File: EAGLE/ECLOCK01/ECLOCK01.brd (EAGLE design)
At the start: 100 x 54 mm, 12 parts

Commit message: FInal version of clock PCB before sending to board house
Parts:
- removed JP1: POWER_JACKCOMBO, SparkFun-Connectors:POWER_JACK_COMBO
- removed L1, L2, L3, L4: WS2812B, adafruit:WS2812B
- added C10, C11, C12, C13, C14, C15, C16, C17, C18, C19, C20, C21, C22, C23, C24, C25, C26, C27, C28, C29, C30, C31, C32, C33, C34, C35, C36, C37, C38, C39, C41, C42, C43, C44, C45, C46, C47, C48, C49, C50, C51, C52, C53, C54, C6, C7, C8, C9: 0.1, TinWhiskers:0805
- added C400, C401: 470, adafruit:PANASONIC_E
- added FID1, FID2: FIDUCIAL, TinWhiskers:FIDUCIAL
- added JP2: USB-MICROB, SparkFun-Connectors:USB-MICROB
- added LED1, LED10, LED11, LED12, LED13, LED14, LED15, LED16, LED17, LED18, LED19, LED2, LED20, LED21, LED22, LED23, LED24, LED25, LED26, LED27, LED28, LED29, LED3, LED30, LED31, LED32, LED33, LED34, LED35, LED36, LED37, LED38, LED39, LED4, LED40, LED41, LED42, LED43, LED44, LED45, LED46, LED47, LED48, LED49, LED5, LED50, LED51, LED52, LED53, LED54, LED6, LED7, LED8, LED9: WS2812B, GinWhiskers - temp stuff:WS2812B
- C1, C2, C3: value CAPACITOR0805 -> 0.1
- C4, C5: value 470 -> 0.1; device adafruit:PANASONIC_E -> TinWhiskers:0805
- U$1: device adafruit:ARDUINO -> GinWhiskers - temp stuff:ARDUINO-UNO
- moved C4 86.1 mm to (5.00, 32.0)
- moved C5 62.9 mm to (8.50, 32.0), turned to 180 degrees
- moved C1 33.5 mm to (7.00, 48.0), turned to 180 degrees
- moved C2 20.2 mm to (15.0, 48.0), turned to 180 degrees
- moved R1 20.1 mm to (28.5, 50.0), turned to 180 degrees
- moved C3 19.0 mm to (23.0, 48.0), turned to 180 degrees
- moved U$1 9.06 mm to (28.0, 1.00)
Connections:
- removed net N$6: L3.2-DOUT, L4.4-DIN
- new net N$10: LED15.2-DOUT, LED16.4-DIN
- new net N$12: LED18.4-DIN, LED53.2-DOUT
- new net N$13: LED19.2-DOUT, LED20.4-DIN
- new net N$14: LED17.4-DIN, LED18.2-DOUT
- new net N$15: LED19.4-DIN, LED8.2-DOUT
- new net N$16: LED47.2-DOUT, LED49.4-DIN
- new net N$17: LED39.2-DOUT, LED50.4-DIN
- new net N$18: LED24.2-DOUT, LED25.4-DIN
- new net N$19: LED25.2-DOUT, LED26.4-DIN
- new net N$2: LED11.2-DOUT, LED12.4-DIN
- new net N$20: LED13.2-DOUT, LED24.4-DIN
- new net N$21: LED27.2-DOUT, LED28.4-DIN
- new net N$22: LED28.2-DOUT, LED29.4-DIN
- new net N$25: LED40.2-DOUT, LED41.4-DIN
- new net N$26: LED20.2-DOUT, LED21.4-DIN
- new net N$27: LED11.4-DIN, LED9.2-DOUT
- new net N$28: LED17.2-DOUT, LED5.4-DIN
- new net N$29: LED4.4-DIN, LED5.2-DOUT
- new net N$30: LED6.2-DOUT, LED7.4-DIN
- new net N$31: LED7.2-DOUT, LED8.4-DIN
- new net N$32: LED21.2-DOUT, LED32.4-DIN
- new net N$33: LED48.4-DIN, LED49.2-DOUT
- new net N$34: LED36.4-DIN, LED48.2-DOUT
- new net N$36: LED37.2-DOUT, LED38.4-DIN
- new net N$37: LED38.2-DOUT, LED39.4-DIN
- new net N$39: LED30.2-DOUT, LED53.4-DIN
- new net N$40: LED34.2-DOUT, LED45.4-DIN
- new net N$41: LED32.2-DOUT, LED33.4-DIN
- new net N$42: LED33.2-DOUT, LED34.4-DIN
- new net N$44: LED31.4-DIN, LED43.2-DOUT
- new net N$45: LED4.2-DOUT, LED6.4-DIN
- new net N$46: LED46.2-DOUT, LED47.4-DIN
- new net N$47: LED45.2-DOUT, LED46.4-DIN
- new net N$48: LED42.2-DOUT, LED44.4-DIN
- new net N$49: LED43.4-DIN, LED44.2-DOUT
- new net N$50: LED30.4-DIN, LED31.2-DOUT
- new net N$51: LED41.2-DOUT, LED42.4-DIN
- new net N$52: LED35.4-DIN, LED36.2-DOUT
- new net N$53: LED35.2-DOUT, LED54.4-DIN
- new net N$54: LED50.2-DOUT, LED51.4-DIN
- new net N$55: LED51.2-DOUT, LED52.4-DIN
- new net N$56: LED23.4-DIN, LED54.2-DOUT
- new net N$58: LED22.4-DIN, LED23.2-DOUT
- new net N$59: LED14.4-DIN, LED3.2-DOUT
- new net N$60: LED10.4-DIN, LED22.2-DOUT
- new net N$61: LED10.2-DOUT, LED9.4-DIN
- new net N$62: LED29.2-DOUT, LED40.4-DIN
- new net N$7: LED12.2-DOUT, LED13.4-DIN
- new net N$8: LED26.2-DOUT, LED37.4-DIN
- new net N$9: LED14.2-DOUT, LED15.4-DIN
- new net VDD: C1.1, C10.1, C11.1, C12.1, C13.1, C14.1, C15.1, C16.1, C17.1, C18.1, C19.1, C2.1, C20.1, C21.1, C22.1, C23.1, C24.1, C25.1, C26.1, C27.1, C28.1, C29.1, C3.1, C30.1, C31.1, C32.1, C33.1, C34.1, C35.1, C36.1, C37.1, C38.1, C39.1, C4.1, C400.+, C401.+, C41.1, C42.1, C43.1, C44.1, C45.1, C46.1, C47.1, C48.1, C49.1, C5.1, C50.1, C51.1, C52.1, C53.1, C54.1, C6.1, C7.1, C8.1, C9.1, JP2.VBUS, LED1.1-VDD, LED10.1-VDD, LED11.1-VDD, LED12.1-VDD, LED13.1-VDD, LED14.1-VDD, LED15.1-VDD, LED16.1-VDD, LED17.1-VDD, LED18.1-VDD, LED19.1-VDD, LED2.1-VDD, LED20.1-VDD, LED21.1-VDD, LED22.1-VDD, LED23.1-VDD, LED24.1-VDD, LED25.1-VDD, LED26.1-VDD, LED27.1-VDD, LED28.1-VDD, LED29.1-VDD, LED3.1-VDD, LED30.1-VDD, LED31.1-VDD, LED32.1-VDD, LED33.1-VDD, LED34.1-VDD, LED35.1-VDD, LED36.1-VDD, LED37.1-VDD, LED38.1-VDD, LED39.1-VDD, LED4.1-VDD, LED40.1-VDD, LED41.1-VDD, LED42.1-VDD, LED43.1-VDD, LED44.1-VDD, LED45.1-VDD, LED46.1-VDD, LED47.1-VDD, LED48.1-VDD, LED49.1-VDD, LED5.1-VDD, LED50.1-VDD, LED51.1-VDD, LED52.1-VDD, LED53.1-VDD, LED54.1-VDD, LED6.1-VDD, LED7.1-VDD, LED8.1-VDD, LED9.1-VDD
- net GND: now also C1.2, C10.2, C11.2, C12.2, C13.2, C14.2, C15.2, C16.2, C17.2, C18.2, C19.2, C2.2, C20.2, C21.2, C22.2, C23.2, C24.2, C25.2, C26.2, C27.2, C28.2, C29.2, C3.2, C30.2, C31.2, C32.2, C33.2, C34.2, C35.2, C36.2, C37.2, C38.2, C39.2, C4.2, C400.-, C401.-, C41.2, C42.2, C43.2, C44.2, C45.2, C46.2, C47.2, C48.2, C49.2, C5.2, C50.2, C51.2, C52.2, C53.2, C54.2, C6.2, C7.2, C8.2, C9.2, JP2.GND, JP2.MT1, JP2.MT2, LED1.3-GND, LED10.3-GND, LED11.3-GND, LED12.3-GND, LED13.3-GND, LED14.3-GND, LED15.3-GND, LED16.3-GND, LED17.3-GND, LED18.3-GND, LED19.3-GND, LED2.3-GND, LED20.3-GND, LED21.3-GND, LED22.3-GND, LED23.3-GND, LED24.3-GND, LED25.3-GND, LED26.3-GND, LED27.3-GND, LED28.3-GND, LED29.3-GND, LED3.3-GND, LED30.3-GND, LED31.3-GND, LED32.3-GND, LED33.3-GND, LED34.3-GND, LED35.3-GND, LED36.3-GND, LED37.3-GND, LED38.3-GND, LED39.3-GND, LED4.3-GND, LED40.3-GND, LED41.3-GND, LED42.3-GND, LED43.3-GND, LED44.3-GND, LED45.3-GND, LED46.3-GND, LED47.3-GND, LED48.3-GND, LED49.3-GND, LED5.3-GND, LED50.3-GND, LED51.3-GND, LED52.3-GND, LED53.3-GND, LED54.3-GND, LED6.3-GND, LED7.3-GND, LED8.3-GND, LED9.3-GND; no longer C4.-, C5.-, JP1.GND, JP1.GND@1, L1.3-GND, L2.3-GND, L3.3-GND, L4.3-GND
- net LED_IN: now also U$1.D13; no longer U$1.D0
- net N$1: now also LED1.4-DIN; no longer L1.4-DIN
- net N$3: now also LED1.2-DOUT, LED2.4-DIN; no longer L1.2-DOUT, L2.4-DIN
- net N$4: now also LED2.2-DOUT, LED3.4-DIN; no longer L2.2-DOUT, L3.4-DIN
- net N$5: now also LED16.2-DOUT, LED27.4-DIN; no longer C4.+, C5.+, JP1.POWER, L1.1-VDD, L2.1-VDD, L3.1-VDD, L4.1-VDD
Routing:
- net GND: track 0.00 -> 271.3 mm, vias 0 -> 62
- net N$1: track 0.00 -> 29.6 mm
- net LED_IN: track 0.00 -> 28.8 mm, vias 0 -> 1
- net N$8: track 0.00 -> 24.5 mm
- net N$5: track 0.00 -> 24.5 mm
- net N$32: track 0.00 -> 24.5 mm
- net N$61: track 0.00 -> 12.5 mm
- net N$29: track 0.00 -> 12.5 mm
- net N$58: track 0.00 -> 12.5 mm
- net N$14: track 0.00 -> 12.5 mm
- net N$52: track 0.00 -> 12.5 mm
- net N$50: track 0.00 -> 12.5 mm
- net N$49: track 0.00 -> 12.5 mm
- net N$33: track 0.00 -> 12.5 mm
- net N$45: track 0.00 -> 11.7 mm, vias 0 -> 2
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- added copper zone on layer 1, net GND
- added copper zone on layer 16, net GND
- added copper zone on layer 1, net VDD
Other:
- board size 100 x 54 mm -> 135 x 55 mm

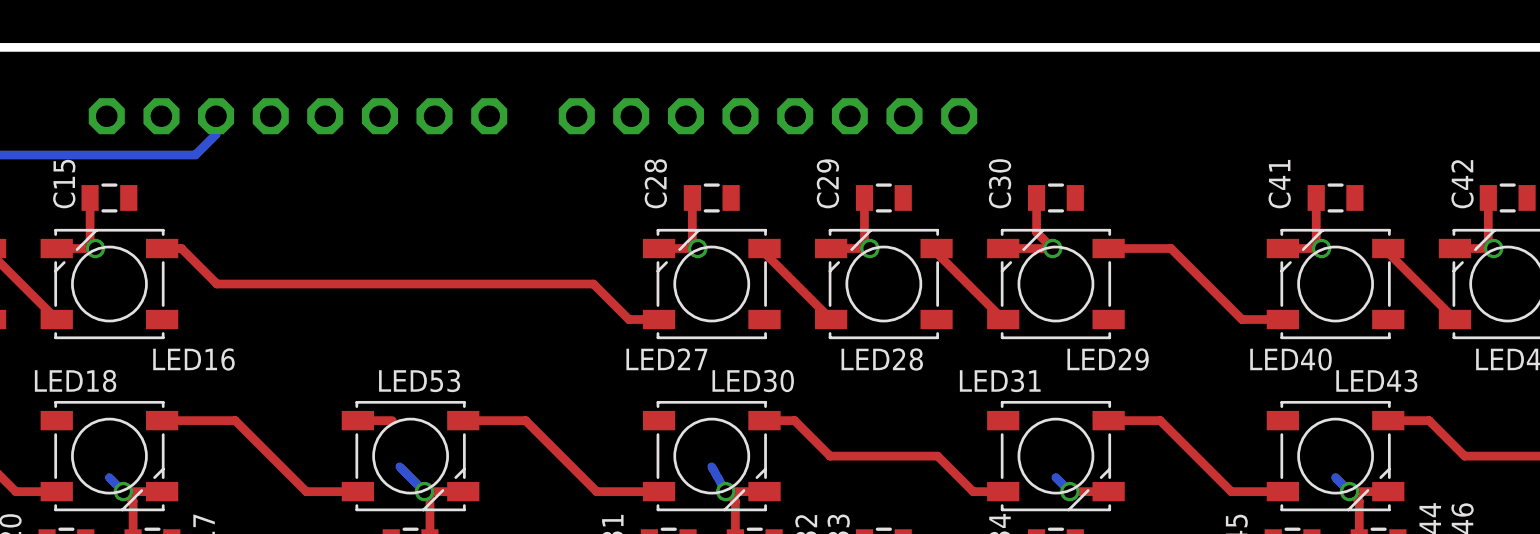
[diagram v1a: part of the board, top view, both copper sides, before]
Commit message: Added two pushbuttons and a connector for the horn
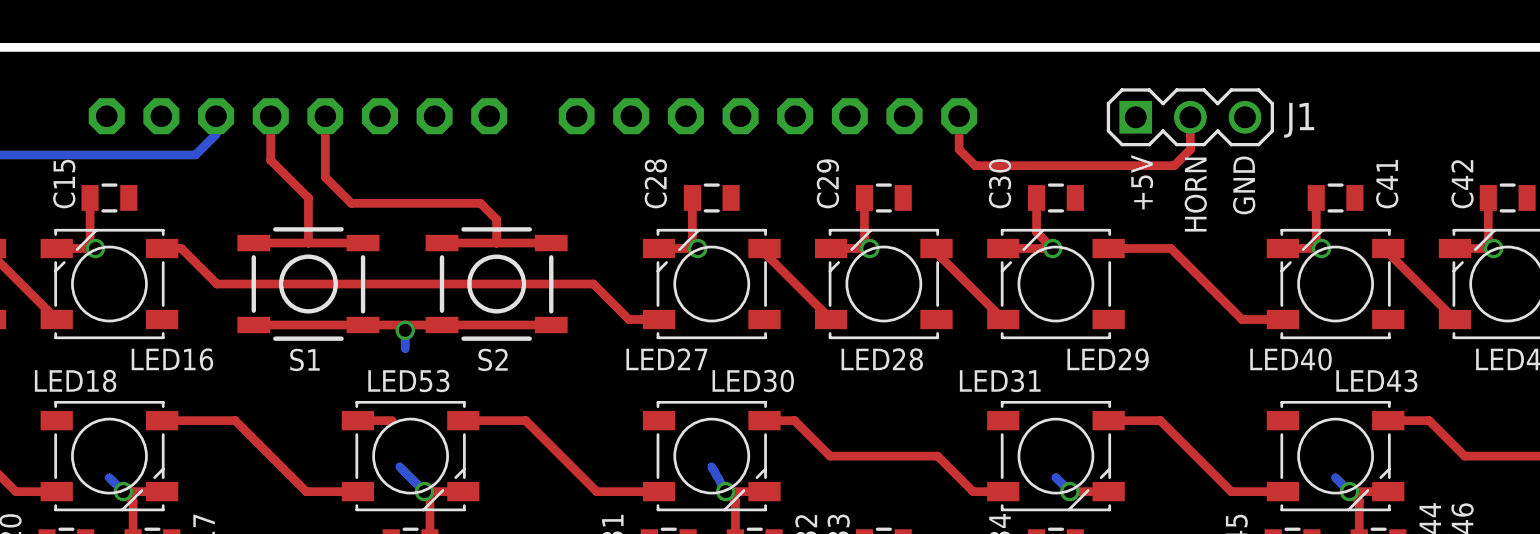
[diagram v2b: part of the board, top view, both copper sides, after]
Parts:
- added J1: (no value), !con-lstb:MA03-1
- added S1, S2: (no value), SparkFun:TACTILE_SWITCH_SMD
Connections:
- net 5V renamed ARD_5V
- new net BTN1: S1.3, S1.4, U$1.D12
- new net BTN2: S2.3, S2.4, U$1.D11
- new net HORN: J1.2, U$1.D0
- net GND: now also J1.3, S1.1, S1.2, S2.1, S2.2
- net VDD: now also J1.1
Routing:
- net BTN2: track 0.00 -> 17.8 mm
- net GND: track 271.3 -> 286.2 mm, vias 62 -> 63
- net HORN: track 0.00 -> 14.4 mm
- net BTN1: track 0.00 -> 11.7 mm
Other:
- board text added: "+5V"
- board text added: "GND"
- board text added: "HORN"
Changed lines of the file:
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@@
 <wire x1="135" y1="55" x2="0" y2="55" width="0.4064" layer="20"/>
 <wire x1="0" y1="55" x2="0" y2="0" width="0.4064" layer="20"/>
+<text x="102" y="50" size="1" layer="21" ratio="11" rot="R270">HORN</text>
+<text x="104.25" y="50" size="1" layer="21" ratio="11" rot="R270">GND</text>
+<text x="99.5" y="50" size="1" layer="21" ratio="11" rot="R270">+5V</text>
 </plain>
 <attributes>
@@
 </variantdefs>
 <classes>
-<class number="0" name="default" width="0" drill="0">
+<class number="0" name="default" width="0.1524" drill="0.3048">
+<clearance class="0" value="0.1524"/>
+</class>
+<class number="1" name="power" width="0" drill="0">
 </class>
 </classes>
@@
 </element>
 <element name="LED16" library="GinWhiskers - temp stuff" package="WS2812B" value="WS2812B" x="52" y="44" smashed="yes">
-<attribute name="NAME" x="53.9125" y="39.9925" size="1" layer="25" ratio="10"/>
+<attribute name="NAME" x="52.9125" y="39.9925" size="1" layer="25" ratio="10"/>
 </element>
 <element name="LED17" library="GinWhiskers - temp stuff" package="WS2812B" value="WS2812B" x="36" y="36" smashed="yes" rot="R180">
@@
 </element>
 <element name="LED53" library="GinWhiskers - temp stuff" package="WS2812B" value="WS2812B" x="66" y="36" smashed="yes" rot="R180">
-<attribute name="NAME" x="64.4125" y="38.9925" size="1" layer="25" ratio="10"/>
+<attribute name="NAME" x="63.9125" y="38.9925" size="1" layer="25" ratio="10"/>
 </element>
 <element name="LED54" library="GinWhiskers - temp stuff" package="WS2812B" value="WS2812B" x="66" y="20" smashed="yes" rot="R180">
@@
 </element>
 <element name="C41" library="TinWhiskers" package="0805" value="0.1" x="109" y="48" smashed="yes" rot="R180">
-<attribute name="NAME" x="106.9" y="47.45" size="1" layer="25" font="vector" ratio="11" rot="R90"/>
+<attribute name="NAME" x="111.9" y="47.45" size="1" layer="25" font="vector" ratio="11" rot="R90"/>
 </element>
 <element name="C42" library="TinWhiskers" package="0805" value="0.1" x="117" y="48" smashed="yes" rot="R180">
@@
 <element name="C54" library="TinWhiskers" package="0805" value="0.1" x="127" y="16" smashed="yes" rot="R180">
 <attribute name="NAME" x="129.9" y="14.95" size="1" layer="25" font="vector" ratio="11" rot="R90"/>
+</element>
+<element name="S1" library="SparkFun" package="TACTILE_SWITCH_SMD" value="" x="61.25" y="44" smashed="yes" rot="R180">
+<attribute name="NAME" x="61.889" y="40.972" size="1" layer="25" rot="R180"/>
+<attribute name="VALUE" x="62.139" y="46.032" size="0.4064" layer="27" rot="R180"/>
+</element>
+<element name="S2" library="SparkFun" package="TACTILE_SWITCH_SMD" value="" x="70" y="44" smashed="yes" rot="R180">
+<attribute name="NAME" x="70.639" y="40.972" size="1" layer="25" rot="R180"/>
+<attribute name="VALUE" x="70.889" y="46.032" size="0.4064" layer="27" rot="R180"/>
+</element>
+<element name="J1" library="!con-lstb" package="MA03-1" value="" x="102.25" y="51.75" smashed="yes">
+<attribute name="NAME" x="106.69" y="51.151" size="1.27" layer="25" ratio="10"/>
 </element>
 </elements>
@@
 <wire x1="6.1" y1="48" x2="5.6" y2="48" width="0.4064" layer="1"/>
 <wire x1="5.6" y1="48" x2="4.55" y2="46.95" width="0.4064" layer="1"/>
+<contactref element="S1" pad="2"/>
+<contactref element="S1" pad="1"/>
+<contactref element="S2" pad="1"/>
+<contactref element="S2" pad="2"/>
+<wire x1="58.71" y1="42.095" x2="63.79" y2="42.095" width="0.4064" layer="1"/>
+<wire x1="72.54" y1="42.095" x2="67.46" y2="42.095" width="0.4064" layer="1"/>
+<wire x1="65.75" y1="41.845" x2="65.75" y2="41" width="0.4064" layer="16"/>
+<via x="65.75" y="41.845" extent="1-16" drill="0.6"/>
+<wire x1="63.79" y1="42.095" x2="65.75" y2="42.095" width="0.4064" layer="1"/>
+<wire x1="65.75" y1="42.095" x2="67.46" y2="42.095" width="0.4064" layer="1"/>
+<wire x1="65.75" y1="41.845" x2="65.75" y2="42.095" width="0.4064" layer="1"/>
+<contactref element="J1" pad="3"/>
 </signal>
 <signal name="VIN">
 <contactref element="U$1" pad="VIN"/>
-</signal>
-<signal name="5V">
-<contactref element="U$1" pad="5V"/>
 </signal>
 <signal name="3V">
@@
 <contactref element="C53" pad="1"/>
 <contactref element="C54" pad="1"/>
+<contactref element="J1" pad="1"/>
 </signal>
 <signal name="N$59">
@@
 <wire x1="5.15" y1="18.35" x2="7" y2="16.5" width="0.4064" layer="1"/>
 </signal>
+<signal name="BTN2">
+<contactref element="S2" pad="3"/>
+<contactref element="S2" pad="4"/>
+<wire x1="67.46" y1="45.905" x2="70" y2="45.905" width="0.4064" layer="1"/>
+<wire x1="70" y1="45.905" x2="72.54" y2="45.905" width="0.4064" layer="1"/>
+<contactref element="U$1" pad="D11"/>
+<wire x1="62.036" y1="51.8" x2="62.036" y2="48.964" width="0.4064" layer="1"/>
+<wire x1="62.036" y1="48.964" x2="63.25" y2="47.75" width="0.4064" layer="1"/>
+<wire x1="63.25" y1="47.75" x2="69.25" y2="47.75" width="0.4064" layer="1"/>
+<wire x1="69.25" y1="47.75" x2="70" y2="47" width="0.4064" layer="1"/>
+<wire x1="70" y1="47" x2="70" y2="45.905" width="0.4064" layer="1"/>
+</signal>
+<signal name="BTN1">
+<contactref element="S1" pad="3"/>
+<contactref element="S1" pad="4"/>
+<wire x1="58.71" y1="45.905" x2="61.25" y2="45.905" width="0.4064" layer="1"/>
+<wire x1="61.25" y1="45.905" x2="63.79" y2="45.905" width="0.4064" layer="1"/>
+<contactref element="U$1" pad="D12"/>
+<wire x1="59.496" y1="51.8" x2="59.496" y2="49.754" width="0.4064" layer="1"/>
+<wire x1="59.496" y1="49.754" x2="61.25" y2="48" width="0.4064" layer="1"/>
+<wire x1="61.25" y1="48" x2="61.25" y2="45.905" width="0.4064" layer="1"/>
+</signal>
+<signal name="ARD_5V">
+<contactref element="U$1" pad="5V"/>
+</signal>
+<signal name="HORN">
+<contactref element="J1" pad="2"/>
+<wire x1="102.25" y1="51.75" x2="102.25" y2="50.25" width="0.4064" layer="1"/>
+<wire x1="102.25" y1="50.25" x2="101.5" y2="49.5" width="0.4064" layer="1"/>
+<contactref element="U$1" pad="D0"/>
+<wire x1="101.5" y1="49.5" x2="92.25" y2="49.5" width="0.4064" layer="1"/>
+<wire x1="92.25" y1="49.5" x2="91.5" y2="50.25" width="0.4064" layer="1"/>
+<wire x1="91.5" y1="51.8" x2="91.5" y2="50.25" width="0.4064" layer="1"/>
+</signal>
 </signals>
